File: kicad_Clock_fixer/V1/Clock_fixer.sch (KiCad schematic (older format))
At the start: 11 parts, among them J1 Conn_01x03, U1 74VHC163, U2 74VHC163, U3 74AHC02, U4 74VHC163, U6 27C128, X1 IQXO-70

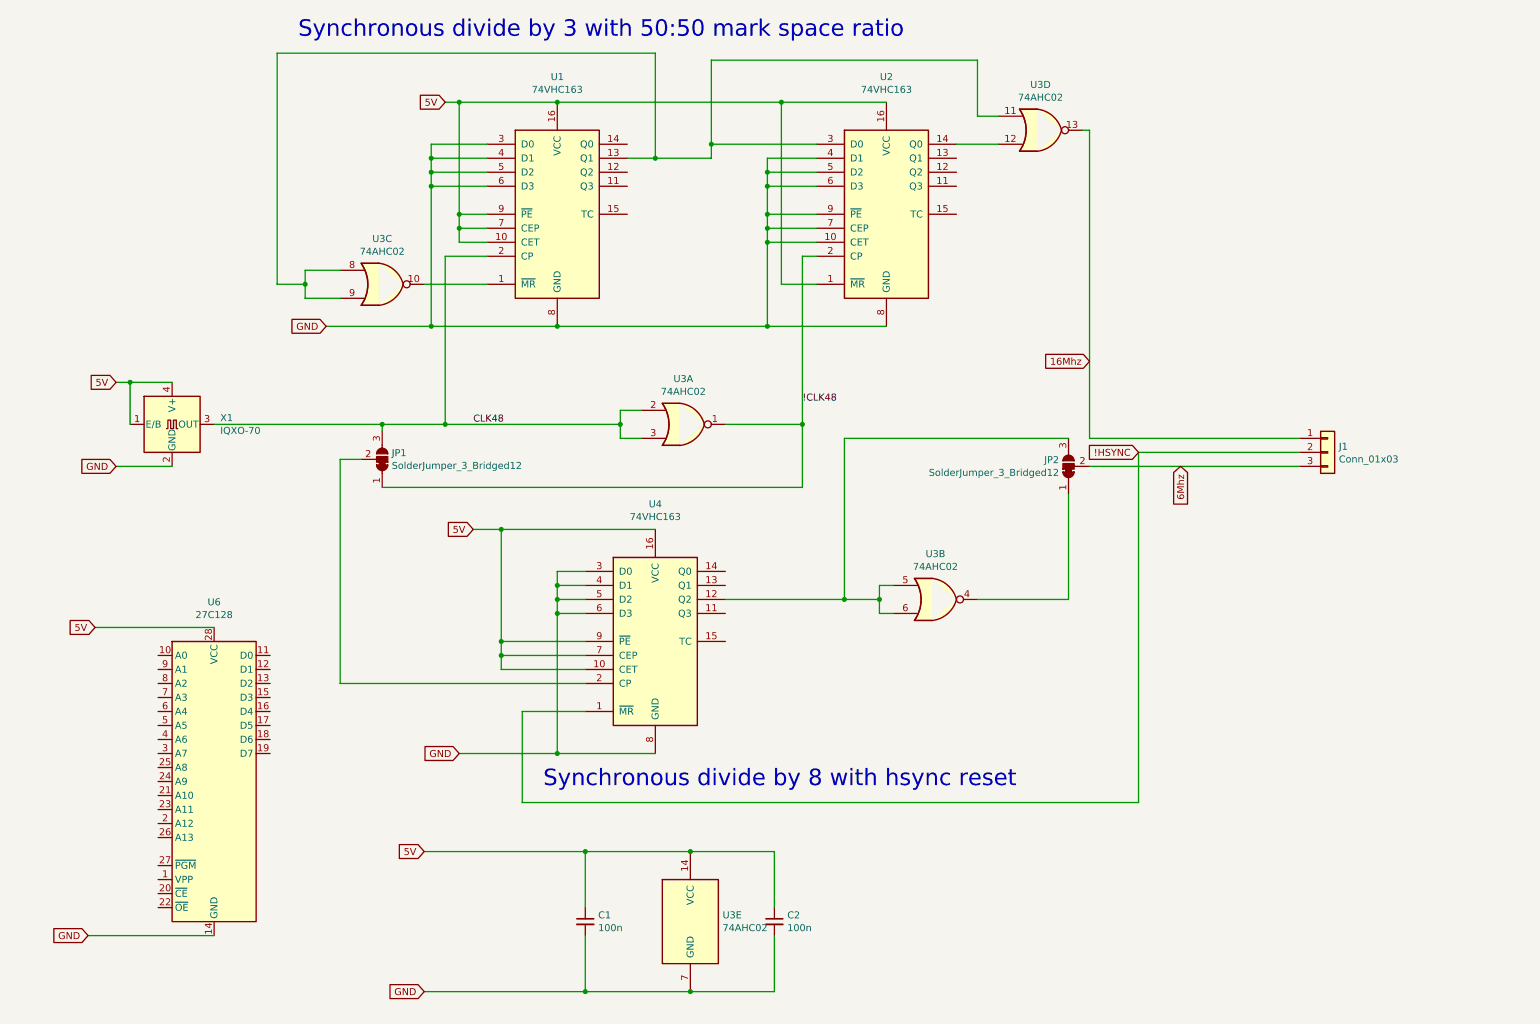
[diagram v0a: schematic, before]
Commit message: Update clock fixer schematic
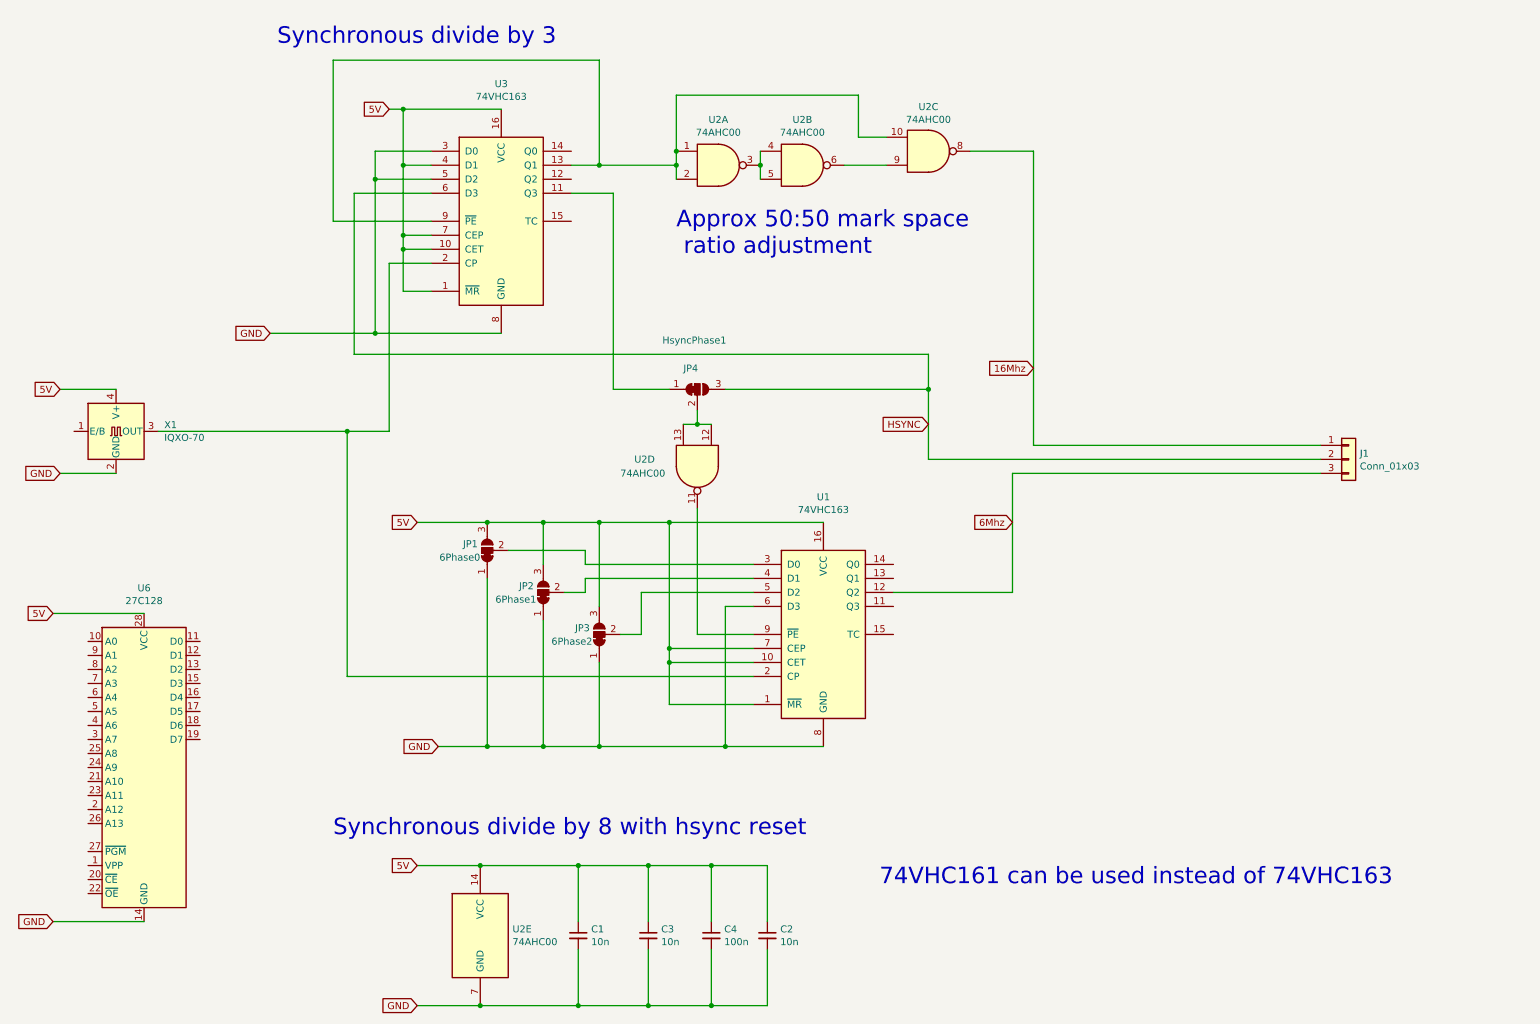
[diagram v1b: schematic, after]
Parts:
- removed U2: 74VHC163, Package_SO:TSSOP-16_4.4x5mm_P0.65mm, symbol 74xx:74LS163
- removed U3: 74AHC02, Package_SO:TSSOP-14_4.4x5mm_P0.65mm, symbol Clock_fixer-rescue:74AHC02-74xx
- added C3: 10n, Capacitor_SMD:C_0603_1608Metric, symbol Device:C_Small
- added C4: 100n, Capacitor_SMD:C_0603_1608Metric, symbol Device:C_Small
- added JP1: 6Phase0, Jumper:SolderJumper-3_P1.3mm_Bridged12_RoundedPad1.0x1.5mm, symbol Jumper:SolderJumper_3_Bridged12
- added JP4: HsyncPhase1, Jumper:SolderJumper-3_P1.3mm_Bridged12_RoundedPad1.0x1.5mm, symbol Jumper:SolderJumper_3_Bridged12
- added U2: 74AHC00, Package_SO:TSSOP-14_4.4x5mm_P0.65mm, symbol 74xx:74HC00
- C1, C2: value 100n -> 10n
- JP2: value SolderJumper_3_Bridged12 -> 6Phase1
- JP3: renamed from JP1; value SolderJumper_3_Bridged12 -> 6Phase2
- X1: footprint Oscillator:Oscillator_SMD_IQD_IQXO70-4Pin_7.5x5.0mm_HandSoldering -> Oscillator:Oscillator_SMD_SeikoEpson_SG8002CE-4Pin_3.2x2.5mm
- renumbered U4 to U1, U1 to U3
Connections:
- net !CLK48 is gone; now on net GND: JP3.1 (A)
- net 16Mhz: now also U2.8
- net 5V: now also JP2.3 (B), JP3.3 (B), U1.1 (~MR), U3.1 (~MR), U3.4 (D1), C3.1, C4.1, JP1.3 (B), U2.14 (VCC); no longer U1.9 (~PE), U3.9 (~PE), X1.1 (E/B)
- net 6Mhz: now also U1.12 (Q2); no longer JP2.2 (C)
- net GND: now also JP2.1 (A), C3.2, C4.2, JP1.1 (A), U2.7 (GND); no longer U1.3 (D0), U1.4 (D1), U1.5 (D2), U3.4 (D1), U3.6 (D3)
- net at U3.13 (Q1): now also U3.9 (~PE), U2.1, U2.10, U2.2
- net at U1.2 (CP): now also U3.2 (CP), X1.3 (OUT); no longer JP3.2 (C)
- net at U3.11 (Q3): now also JP4.1 (A)
- net !HSYNC renamed HSYNC
- net HSYNC: now also U3.6 (D3), JP4.3 (B); no longer U1.1 (~MR)
- removed net CLK48: JP3.3 (B), U3.2 (CP), X1.3 (OUT)
- new net: JP1.2 (C), U1.3 (D0)
- new net: JP2.2 (C), U1.4 (D1)
- new net: JP3.2 (C), U1.5 (D2)
- new net: U1.9 (~PE), U2.11
- new net: U2.6, U2.9
- new net: JP4.2 (C), U2.12, U2.13
- new net: U2.3, U2.4, U2.5
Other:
- note added: "74VHC161 can be used instead of 74VHC163"
- note added: "Approx 50:50 mark space\n ratio adjustment"
- note added: "Synchronous divide by 3"
- note removed: "Synchronous divide by 3 with 50:50 mark space ratio"
- moved on the sheet: C1, C2, J1, JP3, U1, U3, U6, X1
